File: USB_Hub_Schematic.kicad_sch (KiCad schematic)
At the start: 115 parts, among them Q2 BSS84_C114481, Q3 BSS84_C114481, Q4 BSS84_C114481, Q5 BSS84_C114481, U1 USB2517 Chip, U10 TP, U11 TP, U12 TP, U13 TP, U14 TP, U15 TP, U2 USB to microSD, U3 MUX, U4 USB-A F, U5 3.3V CONV, U6 USB-A F, U8 TPS2054B, U9 TP, X1 24MHz, X2 24MHz

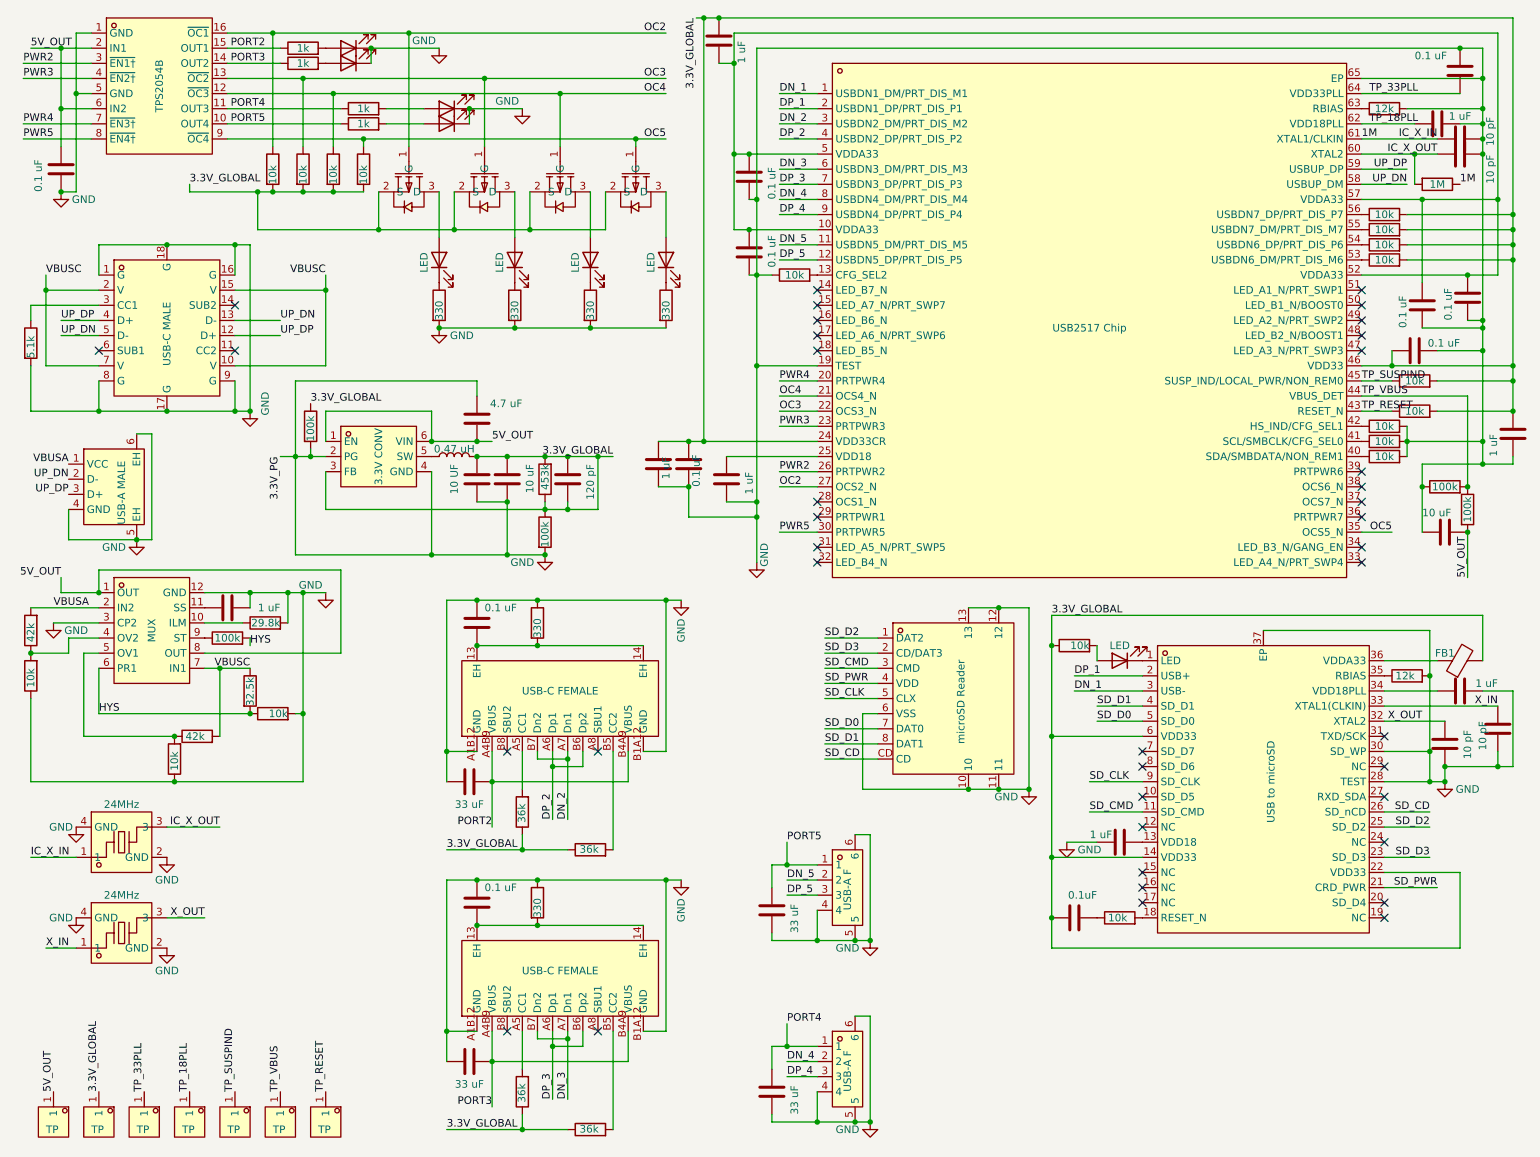
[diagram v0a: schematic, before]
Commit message: Schematic & PCB work
Started PCB layout
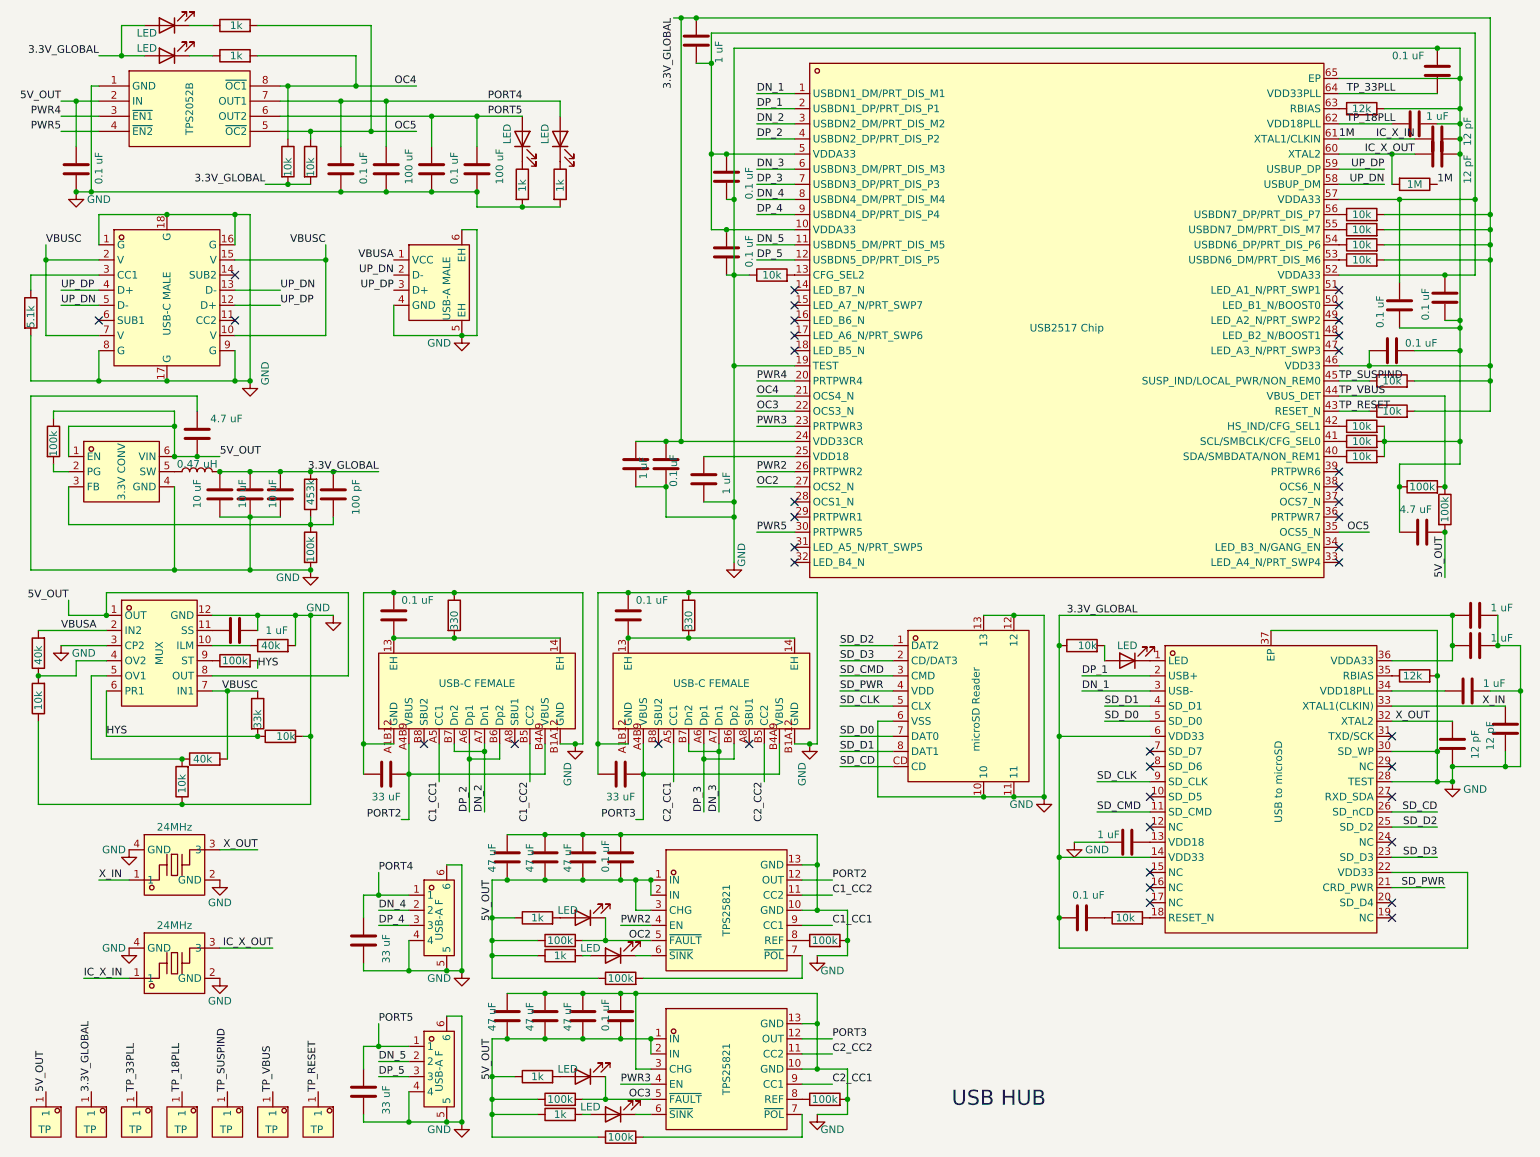
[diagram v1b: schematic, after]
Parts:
- removed C30: 1 uF, symbol Device:C
- removed D2, D3, D4, D5, D6, D7, D8, D9: LED, symbol Device:LED
- removed FB1: FerriteBead, symbol Device:FerriteBead
- removed Q2, Q3, Q4, Q5: BSS84_C114481, lcsc_easyeda:SOT-23-3_L2.9-W1.6-P1.90-LS2.8-BR, symbol lcsc_easyeda:BSS84_C114481
- removed R32, R33: 10k, symbol Device:R
- removed R35, R36, R39, R40: 330, symbol Device:R
- removed R42, R43, R44, R45: 1k, symbol Device:R
- removed U8: TPS2054B, lcsc_easyeda:SOP-16_L9.9-W3.9-P1.27-LS6.1-BL, symbol lcsc_easyeda:TPS2054BDR
- removed USB5: USB-C FEMALE, lcsc_easyeda:USB-C-SMD_TYPE-C-16PIN-2MD-073, symbol lcsc_easyeda:TYPE-C16PIN2MD
- added C12, C13, C17, C33, C38, C39: 47 uF, Capacitor_SMD:C_0805_2012Metric, symbol Device:C
- added C37, C40, C41, C42, C44: 0.1 uF, Capacitor_SMD:C_0603_1608Metric, symbol Device:C
- added C43, C45: 100 uF, Capacitor_SMD:C_1206_3216Metric, symbol Device:C
- added C46, C47: 1 uF, Capacitor_SMD:C_0805_2012Metric, symbol Device:C
- added D10, D11, D12, D13, D14, D15, D16, D17: LED, LED_SMD:LED_0805_2012Metric, symbol Device:LED
- added R1, R2, R54, R56: 100k, Resistor_SMD:R_0603_1608Metric, symbol Device:R
- added R21, R53, R55, R57: 1k, Resistor_SMD:R_0603_1608Metric, symbol Device:R
- added R3, R4: 10k, Resistor_SMD:R_0603_1608Metric, symbol Device:R
- added U16, U17: TPS25821, lcsc_easyeda:WSON-12_L3.0-W2.0-P0.5-BL-EP, symbol lcsc_easyeda:TPS25821DSSR
- added U7: TPS2052B, lcsc_easyeda:SOIC-8_L4.9-W3.9-P1.27-LS6.0-BL, symbol lcsc_easyeda:TPS2052BD
- added USB2: USB-C FEMALE, lcsc_easyeda:USB-C-SMD_TYPE-C-16PIN-2MD-073, symbol lcsc_easyeda:TYPE-C16PIN2MD
- C1: value 0.1uF -> 0.1 uF; footprint (none) -> Capacitor_SMD:C_0603_1608Metric
- C10, C11, C23, C24, C25, C29, C32, C36, C9: footprint (none) -> Capacitor_SMD:C_0603_1608Metric
- C14, C2, C21, C3: value 10 pF -> 12 pF; footprint (none) -> Capacitor_SMD:C_0603_1608Metric
- C15: value 0.1 uF -> 10 uF; footprint (none) -> Capacitor_SMD:C_0805_2012Metric
- C16, C18, C19, C20, C22, C26, C27, C31, C34, C35, C4, C5, C7: footprint (none) -> Capacitor_SMD:C_0805_2012Metric
- C28: value 10 uF -> 4.7 uF; footprint (none) -> Capacitor_SMD:C_0805_2012Metric
- C6: value 10 UF -> 10 uF; footprint (none) -> Capacitor_SMD:C_0805_2012Metric
- C8: value 120 pF -> 100 pF; footprint (none) -> Capacitor_SMD:C_0603_1608Metric
- D1: footprint (none) -> LED_SMD:LED_0805_2012Metric
- L1: footprint (none) -> Inductor_SMD:L_1008_2520Metric
- R10: value 32.5k -> 33k; footprint (none) -> Resistor_SMD:R_0603_1608Metric
- R11, R13, R15, R16, R17, R18, R19, R20, R24, R25, R26, R27, R28, R29, R34, R37, R38, R41, R46, R47, R6, R7, R8: footprint (none) -> Resistor_SMD:R_0603_1608Metric
- R12, R14: value 42k -> 40k; footprint (none) -> Resistor_SMD:R_0603_1608Metric
- R22, R48: footprint (none) -> Resistor_SMD:R_1206_3216Metric
- R23, R52: value 36k -> 1k; footprint Resistor_SMD:R_01005_0402Metric -> Resistor_SMD:R_0603_1608Metric
- R30, R31: value 10k -> 1k; footprint (none) -> Resistor_SMD:R_0603_1608Metric
- R49: value 36k -> 100k; footprint Resistor_SMD:R_01005_0402Metric -> Resistor_SMD:R_0603_1608Metric
- R5: footprint Resistor_SMD:R_01005_0402Metric -> Resistor_SMD:R_0603_1608Metric
- R50: value 36k -> 330; footprint Resistor_SMD:R_01005_0402Metric -> Resistor_SMD:R_1206_3216Metric
- R51: value 330 -> 100k; footprint (none) -> Resistor_SMD:R_0603_1608Metric
- R9: value 29.8k -> 40k; footprint (none) -> Resistor_SMD:R_0603_1608Metric
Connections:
- net 3.3V_GLOBAL: now also C15.2, U2.36 (VDDA33), C46.1, C47.1, D16.2 (A), D17.2 (A), R3.2, R4.2; no longer C8.1, R18.1, R19.1, R20.1, R23.1, R30.2, R31.2, R49.1, R50.1, R52.1, U5.3 (FB)
- net 5V_OUT: now also R20.1, R23.1, R49.1, R51.1, R52.1, C12.2, C13.2, C17.2, C33.2, C37.2, C38.2, C39.2, C40.2, C41.1, R53.1, R54.1, R55.1, R56.1, U16.1 (IN), U16.2 (IN), U16.3 (CHG), U17.1 (IN), U17.2 (IN), U7.2 (IN); no longer C15.2
- net DN_3: now also USB2.A7 (Dn1), USB2.B7 (Dn2)
- net DP_3: now also USB2.A6 (Dp1), USB2.B6 (Dp2)
- net GND: now also R50.1, C12.1, C13.1, C17.1, C33.1, C37.1, C38.1, C39.1, C40.1, C41.2, C42.2, C43.2, C44.2, C45.2, C46.2, C47.2, R1.2, R2.2, R21.2, R57.2, U16.10 (GND), U16.13 (GND), U17.10 (GND), U17.13 (GND), U17.3 (CHG), U7.1 (GND), USB2.A1B12 (GND), USB2.B1A12 (GND); no longer R20.2, R51.1, U5.2 (PG)
- net OC2: now also R51.2, D11.1 (K), U16.5 (~{FAULT})
- net OC3: now also D12.1 (K), R54.2, U17.5 (~{FAULT})
- net OC4: now also R31.2, R3.1, U7.8 (~{OC1}); no longer R31.1
- net OC5: now also R30.2, R4.1, U7.5 (~{OC2}); no longer R30.1
- net PORT2: now also U16.12 (OUT)
- net PORT3: now also U17.12 (OUT), USB2.A4B9 (VBUS), USB2.B4A9 (VBUS)
- net PORT4: now also C42.1, C43.1, D15.2 (A), U7.7 (OUT1)
- net PORT5: now also C44.1, C45.1, D14.2 (A), U7.6 (OUT2)
- net PWR2: now also U16.4 (EN)
- net PWR3: now also U17.4 (EN)
- net PWR4: now also U7.3 (~{EN1})
- net PWR5: now also U7.4 (~{EN2})
- net at R50.2: now also C11.2, USB2.13 (EH), USB2.14 (EH)
- net at R49.2: now also U16.7 (~{POL}); no longer USB1.A5 (CC1)
- net at R23.2: now also D10.2 (A); no longer USB1.B5 (CC2)
- net at R52.2: now also D11.2 (A)
- new net: C8.1, R18.1, R19.1, U5.3 (FB)
- new net: R2.1, U17.8 (REF)
- new net: R20.2, U5.2 (PG)
- new net: D17.1 (K), R30.1
- new net: R56.2, U17.7 (~{POL})
- new net: D14.1 (K), R21.1
- new net: D13.1 (K), U17.6 (~{SINK})
- new net: D13.2 (A), R55.2
- new net: D12.2 (A), R53.2
- new net: D10.1 (K), U16.6 (~{SINK})
- new net: D16.1 (K), R31.1
- new net: R1.1, U16.8 (REF)
- new net: D15.1 (K), R57.1
- new net C1_CC1: U16.9 (CC1), USB1.A5 (CC1)
- new net C1_CC2: U16.11 (CC2), USB1.B5 (CC2)
- new net C2_CC1: U17.9 (CC1), USB2.A5 (CC1)
- new net C2_CC2: U17.11 (CC2), USB2.B5 (CC2)
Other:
- note added: "USB HUB"

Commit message: Footprint Fix
Reupload parts folder
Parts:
- removed C10, C11: 0.1 uF, Capacitor_SMD:C_0603_1608Metric, symbol Device:C
- removed C16: 33 uF, Capacitor_SMD:C_0805_2012Metric, symbol Device:C
- removed R22, R50: 330, Resistor_SMD:R_1206_3216Metric, symbol Device:R
- removed U4, U6: USB-A F, lcsc_easyeda:USB-A-TH_USB1125-GF-B, symbol lcsc_easyeda:USB1125-GF-B
- removed USB1, USB2: USB-C FEMALE, lcsc_easyeda:USB-C-SMD_TYPE-C-16PIN-2MD-073, symbol lcsc_easyeda:TYPE-C16PIN2MD
- added C30, C48: 33 uF, Capacitor_SMD:C_0805_2012Metric, symbol Device:C
- added C49: 0.1 uF, Capacitor_SMD:C_0603_1608Metric, symbol Device:C
- added R32, R33: 330, Resistor_SMD:R_0603_1608Metric, symbol Device:R
- added USB5, USB8: USB-C F, lcsc_easyeda:TYPE-C-TH_TYPE-C-14P-CC-2.6, symbol lcsc_easyeda:TYPE-C14PCC-2.6
- added USB6, USB7: USB-A F, lcsc_easyeda:USB-A-TH_USB-226-BRY, symbol lcsc_easyeda:USB-226-BRY
- C18: value 33 uF -> 0.1 uF; footprint Capacitor_SMD:C_0805_2012Metric -> Capacitor_SMD:C_0603_1608Metric
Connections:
- net C1_CC1: now also USB5.A5 (CC1)
- net C1_CC2: now also USB5.B5 (CC2)
- net C2_CC1: now also USB8.A5 (CC1)
- net C2_CC2: now also USB8.B5 (CC2)
- net DN_2: now also USB5.A7 (DN1), USB5.B7 (DN2)
- net DN_3: now also USB8.A7 (DN1), USB8.B7 (DN2)
- net DN_4: now also USB6.2 (D-)
- net DN_5: now also USB7.2 (D-)
- net DP_2: now also USB5.A6 (DP1), USB5.B6 (DP2)
- net DP_3: now also USB8.A6 (DP1), USB8.B6 (DP2)
- net DP_4: now also USB6.3 (D+)
- net DP_5: now also USB7.3 (D+)
- net GND: now also C19.1, C30.2, C48.2, C49.2, R32.2, R33.2, USB5.A1 (GND), USB5.A12 (GND), USB5.B1 (GND), USB5.B12 (GND), USB6.4 (GND), USB6.5 (EH), USB7.4 (GND), USB7.5 (EH), USB8.A1 (GND), USB8.A12 (GND), USB8.B1 (GND), USB8.B12 (GND); no longer C19.2
- net PORT2: now also C19.2, USB5.A4 (VBUS), USB5.A9 (VBUS), USB5.B4 (VBUS), USB5.B9 (VBUS)
- net PORT3: now also USB8.A4 (VBUS), USB8.A9 (VBUS), USB8.B4 (VBUS), USB8.B9 (VBUS)
- net PORT4: now also C30.1, USB6.1 (VCC); no longer C18.1
- net PORT5: now also C48.1, USB7.1 (VCC); no longer C19.1
- new net: C49.1, R33.1, USB8.SH1, USB8.SH2
- new net: C18.1, R32.1, USB5.SH1, USB5.SH2
- no-connect marks 40 -> 36

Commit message: PCB Layout
Initial layout finished, subject to routing
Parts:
- removed R5: 5.1k, Resistor_SMD:R_0603_1608Metric, symbol Device:R
- removed USB3: USB-A MALE, lcsc_easyeda:USB-A-TH_XBDM-9101-018, symbol lcsc_easyeda:XBDM-9101-018
- removed USB4: USB-C MALE, lcsc_easyeda:USB-C-SMD_918-118A2021Y40006, symbol lcsc_easyeda:918-118A2021Y40006
- added J1: USB-C, Connector_Wire:SolderWire-0.1sqmm_1x04_P3.6mm_D0.4mm_OD1mm_Relief, symbol Connector_Generic_Shielded:Conn_01x04_Shielded
- added J2: USB-A, Connector_Wire:SolderWire-0.1sqmm_1x04_P3.6mm_D0.4mm_OD1mm_Relief, symbol Connector_Generic_Shielded:Conn_01x04_Shielded
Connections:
- net GND: now also J1.4 (Pin_4), J1.SH (Shield), J2.4 (Pin_4), J2.SH (Shield)
- net UP_DN: now also J1.2 (Pin_2), J2.2 (Pin_2)
- net UP_DP: now also J1.3 (Pin_3), J2.3 (Pin_3)
- net VBUSA: now also J2.1 (Pin_1)
- net VBUSC: now also J1.1 (Pin_1)
- no-connect marks 36 -> 33

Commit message: Routing
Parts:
- removed R37: 10k, Resistor_SMD:R_0603_1608Metric, symbol Device:R
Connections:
- net TP_SUSPIND is gone; now on net 3.3V_GLOBAL: U1.45 (SUSP_IND/LOCAL_PWR/NON_REM0), U13.1
- net 5V_OUT: now also U17.3 (CHG)
- net GND: no longer U17.3 (CHG)

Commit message: Routing
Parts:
- C1, C14, C18, C2, C21, C23, C24, C25, C29, C3, C32, C36, C37, C40, C41, C42, C44, C49, C8, C9: footprint Capacitor_SMD:C_0603_1608Metric -> Capacitor_SMD:C_0402_1005Metric
- C20, C22, C26, C27, C28, C31, C35, C4, C46, C47, C5: footprint Capacitor_SMD:C_0805_2012Metric -> Capacitor_SMD:C_0603_1608Metric
- D1, D10, D11, D12, D13, D14, D15, D16, D17: footprint LED_SMD:LED_0805_2012Metric -> LED_SMD:LED_0603_1608Metric
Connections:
- net OC4: now also R30.2, R4.1, U7.5 (~{OC2}); no longer R3.1, R31.2, U7.8 (~{OC1})
- net OC5: now also R3.1, R31.2, U7.8 (~{OC1}); no longer R30.2, R4.1, U7.5 (~{OC2})
- net PORT4: now also C44.1, C45.1, D14.2 (A), U7.6 (OUT2); no longer C42.1, C43.1, D15.2 (A), U7.7 (OUT1)
- net PORT5: now also C42.1, C43.1, D15.2 (A), U7.7 (OUT1); no longer C44.1, C45.1, D14.2 (A), U7.6 (OUT2)
- net PWR4: now also U7.4 (~{EN2}); no longer U7.3 (~{EN1})
- net PWR5: now also U7.3 (~{EN1}); no longer U7.4 (~{EN2})

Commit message: More routing
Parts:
- removed C14, C2, C21, C3: 12 pF, Capacitor_SMD:C_0402_1005Metric, symbol Device:C
- removed C26, C27, C46, C47: 1 uF, Capacitor_SMD:C_0603_1608Metric, symbol Device:C
- removed C34: 33 uF, Capacitor_SMD:C_0805_2012Metric, symbol Device:C
- removed C49: 0.1 uF, Capacitor_SMD:C_0402_1005Metric, symbol Device:C
- removed D1: LED, LED_SMD:LED_0603_1608Metric, symbol Device:LED
- removed R33: 330, Resistor_SMD:R_0603_1608Metric, symbol Device:R
- removed R48: 1M, Resistor_SMD:R_1206_3216Metric, symbol Device:R
- removed R6, R8: 10k, Resistor_SMD:R_0603_1608Metric, symbol Device:R
- removed R7: 12k, Resistor_SMD:R_0603_1608Metric, symbol Device:R
- removed U2: USB to microSD, lcsc_easyeda:QFN-36_L6.0-W6.0-P0.50-EP4.2, symbol lcsc_easyeda:USB2244I-AEZG-06-TR
- removed USB5, USB8: USB-C F, lcsc_easyeda:TYPE-C-TH_TYPE-C-14P-CC-2.6, symbol lcsc_easyeda:TYPE-C14PCC-2.6
- removed X1, X2: 24MHz, lcsc_easyeda:CRYSTAL-SMD_4P-L2.0-W1.6-BL-A, symbol lcsc_easyeda:XL7EL89CKI-111YLC-24M
- added C50: 33 uF, Capacitor_SMD:C_0805_2012Metric, symbol Device:C
- added C51: 0.1 uF, Capacitor_SMD:C_0402_1005Metric, symbol Device:C
- added D2: LED, LED_SMD:LED_0603_1608Metric, symbol Device:LED
- added R35: 330, Resistor_SMD:R_0603_1608Metric, symbol Device:R
- added R5: 1k, Resistor_SMD:R_0603_1608Metric, symbol Device:R
- added R50, R58: 10k, Resistor_SMD:R_0603_1608Metric, symbol Device:R
- added U4: USB to microSD, lcsc_easyeda:SSOP-16_L4.9-W3.9-P0.64-LS6.0-BL, symbol lcsc_easyeda:GL823K-HCY04
- added USB1, USB2: USB-C F, lcsc_easyeda:USB-C-SMD_GT-USB-7100A, symbol lcsc_easyeda:GT-USB-7100A
- added X3: 24MHz Osc, lcsc_easyeda:OSC-SMD_4P-L3.2-W2.5-CJ13-320001210A20, symbol lcsc_easyeda:OW2EL89CENUXFMYLC-24M
- C1: value 0.1 uF -> 1 uF; footprint Capacitor_SMD:C_0402_1005Metric -> Capacitor_SMD:C_0603_1608Metric
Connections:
- net 5V_OUT: now also U4.10 (5V)
- net C1_CC1: now also USB1.A5 (CC1)
- net C1_CC2: now also USB1.B5 (CC2)
- net C2_CC1: now also USB2.A5 (CC1)
- net C2_CC2: now also USB2.B5 (CC2)
- net DN_1: now also U4.16 (DM)
- net DN_2: now also U1.4 (USBDN2_DP/PRT_DIS_P2), USB1.A7 (D-); no longer U1.3 (USBDN2_DM/PRT_DIS_M2)
- net DN_3: now also U1.7 (USBDN3_DP/PRT_DIS_P3), USB2.A7 (D-); no longer U1.6 (USBDN3_DM/PRT_DIS_M3)
- net DP_1: now also U4.15 (DP)
- net DP_2: now also U1.3 (USBDN2_DM/PRT_DIS_M2), USB1.A6 (D+); no longer U1.4 (USBDN2_DP/PRT_DIS_P2)
- net DP_3: now also U1.6 (USBDN3_DM/PRT_DIS_M3), USB2.A6 (D+); no longer U1.7 (USBDN3_DP/PRT_DIS_P3)
- net GND: now also C1.2, C15.2, C31.1, C32.1, C35.1, C36.1, C6.2, C7.2, C8.2, D16.2 (A), D17.2 (A), J1.1 (Pin_1), L1.2, R18.2, R24.2, R25.2, R26.2, R3.2, R4.2, R41.2, R46.2, U1.24 (VDD33CR), U1.45 (SUSP_IND/LOCAL_PWR/NON_REM0), U1.46 (VDD33), U10.1, U13.1, C50.1, C51.2, R35.2, R5.2, R50.2, R58.2, U4.1 (VSS), U4.14 (VSS), USB1.A12 (GND), USB1.B12 (GND), USB2.A12 (GND), USB2.B12 (GND), X3.2 (GND), X3.4 (VDD); no longer J1.4 (Pin_4)
- net PORT2: now also USB1.A9 (VBUS), USB1.B9 (VBUS)
- net PORT3: now also C50.2, USB2.A9 (VBUS), USB2.B9 (VBUS)
- net SD_CLK: now also U4.4 (CLK)
- net SD_CMD: now also U4.5 (CMD)
- net SD_D0: now also U4.3 (D0)
- net SD_D1: now also U4.2 (D1)
- net SD_D2: now also U4.7 (D2)
- net SD_D3: now also U4.6 (D3)
- net SD_PWR: now also U4.8 (PMOS)
- net UP_DN: now also J1.3 (Pin_3); no longer J1.2 (Pin_2)
- net UP_DP: now also J1.2 (Pin_2); no longer J1.3 (Pin_3)
- net VBUSC: now also J1.4 (Pin_4); no longer J1.1 (Pin_1)
- net at C18.1, R32.1: now also USB1.EH1, USB1.EH2
- net at U1.47 (LED_A3_N/PRT_SWP3): now also R58.1
- net at U1.49 (LED_A2_N/PRT_SWP2): now also R50.1
- net 1M renamed CLKIN
- net CLKIN: now also X3.3 (OutPut)
- removed net 3.3V_GLOBAL: C1.1, C15.2, C31.1, C32.1, C35.1, C36.1, C6.2, C7.2, C8.2, D16.2 (A), D17.2 (A), L1.2, R18.2, R24.2, R25.2, R26.2, R3.2, R4.2, R41.2, R46.2, U1.24 (VDD33CR), U1.45 (SUSP_IND/LOCAL_PWR/NON_REM0), U1.46 (VDD33), U10.1, U13.1
- net IC_X_OUT: no longer names the net of U1.60 (XTAL2)
- net SD_CD: no longer names the net of Card1.CD
- new net: C1.1, U4.13 (VDDA), U4.9 (VDD)
- new net: C51.1, R35.1, USB2.EH1, USB2.EH2
- new net: D2.1 (K), R5.1
- new net: D2.2 (A), U4.12 (LED)
- no-connect marks 33 -> 22

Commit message: Routing continued
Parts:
- removed C5: 4.7 uF, Capacitor_SMD:C_0603_1608Metric, symbol Device:C
- removed C7: 10 uF, Capacitor_SMD:C_0805_2012Metric, symbol Device:C
- removed C8: 100 pF, Capacitor_SMD:C_0402_1005Metric, symbol Device:C
- removed L1: 0.47 uH, Inductor_SMD:L_1008_2520Metric, symbol Device:L
- removed R18: 453k, Resistor_SMD:R_0603_1608Metric, symbol Device:R
- removed R19: 100k, Resistor_SMD:R_0603_1608Metric, symbol Device:R
- removed U5: 3.3V CONV, lcsc_easyeda:VSON-6_L1.5-W1.5-P0.50-TL, symbol lcsc_easyeda:TPS62827ADMQR
- added C16, C21: 10 uF, Capacitor_SMD:C_0805_2012Metric, symbol Device:C
- added C26: 100 pF, Capacitor_SMD:C_0402_1005Metric, symbol Device:C
- added L2: 0.47 uH, Inductor_SMD:L_1008_2520Metric, symbol Device:L
- added R22: 100k, Resistor_SMD:R_0603_1608Metric, symbol Device:R
- added R42: 10k, Resistor_SMD:R_0603_1608Metric, symbol Device:R
- added U8: 3.3V CONV, lcsc_easyeda:VSON-6_L1.5-W1.5-P0.50-TL, symbol lcsc_easyeda:TPS62827ADMQR
- C6: value 10 uF -> 4.7 uF; footprint Capacitor_SMD:C_0805_2012Metric -> Capacitor_SMD:C_0603_1608Metric
- R20: value 100k -> 453k
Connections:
- net 5V_OUT: now also C6.1, U8.1 (EN), U8.6 (VIN); no longer R20.1
- net GND: now also J1.4 (Pin_4), C16.1, C21.1, R22.2, U8.4 (GND); no longer C15.2, C31.1, C32.1, C35.1, C36.1, C6.1, D16.2 (A), D17.2 (A), J1.1 (Pin_1), R24.2, R25.2, R26.2, R3.2, R4.2, R41.2, R46.2, R50.2, R58.2, U1.24 (VDD33CR), U1.45 (SUSP_IND/LOCAL_PWR/NON_REM0), U1.46 (VDD33), U10.1, U13.1, X3.4 (VDD)
- net UP_DN: now also J1.2 (Pin_2); no longer J1.3 (Pin_3)
- net UP_DP: now also J1.3 (Pin_3); no longer J1.2 (Pin_2)
- net VBUSC: now also J1.1 (Pin_1); no longer J1.4 (Pin_4)
- net 3.3V_GLOBAL: now reaches R20.2
- net 3.3V_GLOBAL: now also C15.2, C31.1, C32.1, C35.1, C36.1, D16.2 (A), D17.2 (A), R24.2, R25.2, R26.2, R3.2, R4.2, R41.2, R46.2, R50.2, R58.2, U1.24 (VDD33CR), U1.46 (VDD33), U10.1, X3.4 (VDD), C16.2, C21.2, C26.2, L2.2, R42.2
- new net: C26.1, R20.1, R22.1, U8.3 (FB)
- new net: L2.1, U8.5 (SW)
- new net TP_SUSPIND: R42.1, U1.45 (SUSP_IND/LOCAL_PWR/NON_REM0), U13.1
- no-connect marks 22 -> 23
